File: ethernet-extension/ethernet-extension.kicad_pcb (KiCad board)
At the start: 2 copper layers, 56 x 30.4 mm, 43 parts, among them J1 Wuerth_7499010121A, J2 East, J3 West, U1 W5500, Y1 25MHz

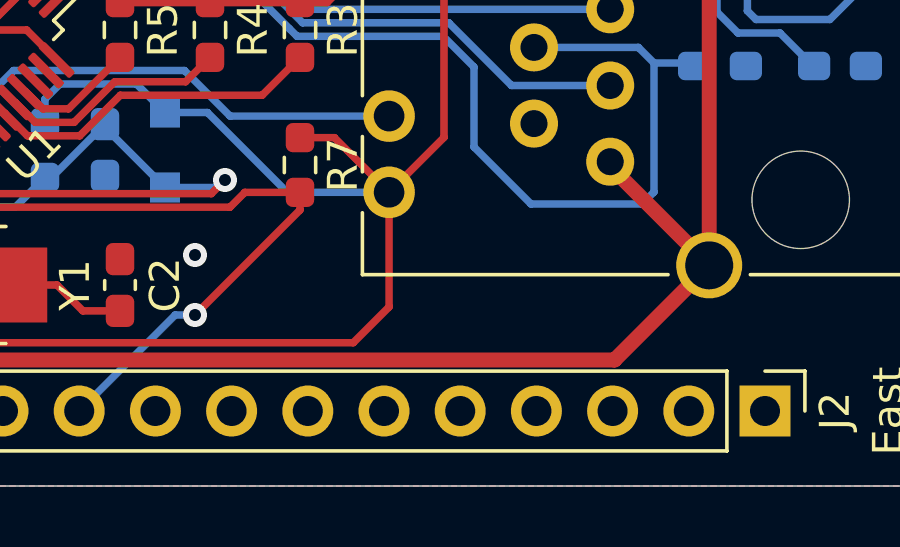
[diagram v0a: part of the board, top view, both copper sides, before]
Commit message: Added Panel Module to build
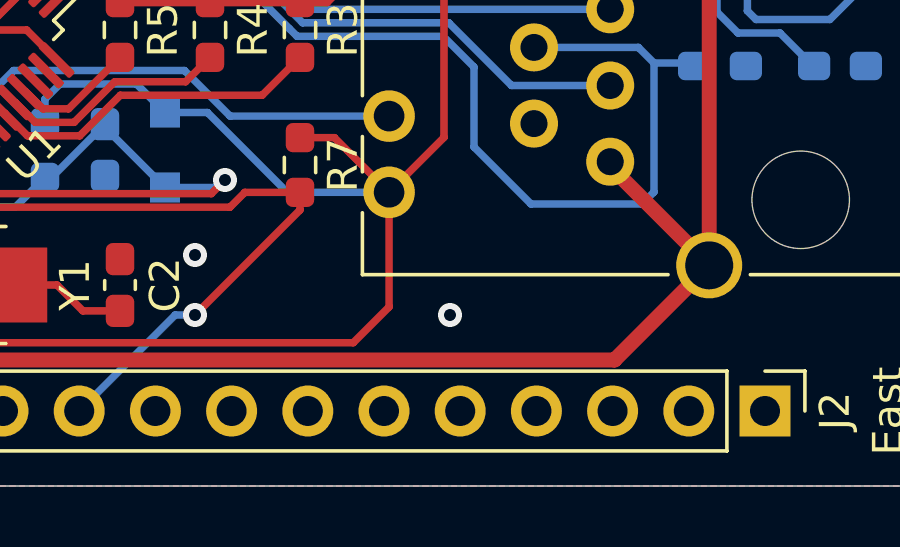
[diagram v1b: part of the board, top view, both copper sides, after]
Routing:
- net GND: vias 5 -> 6

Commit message: Added OpenHardware Logo to PCBs
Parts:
- added G2: Logo_Open_Hardware_Small, Symbol:OSHW-Logo2_7.3x6mm_SilkScreen, B.Cu at (152.5, 106.0)

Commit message: Migrate Ethernet, SoC, Metering Modules to KiCad6
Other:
- net class Default removed

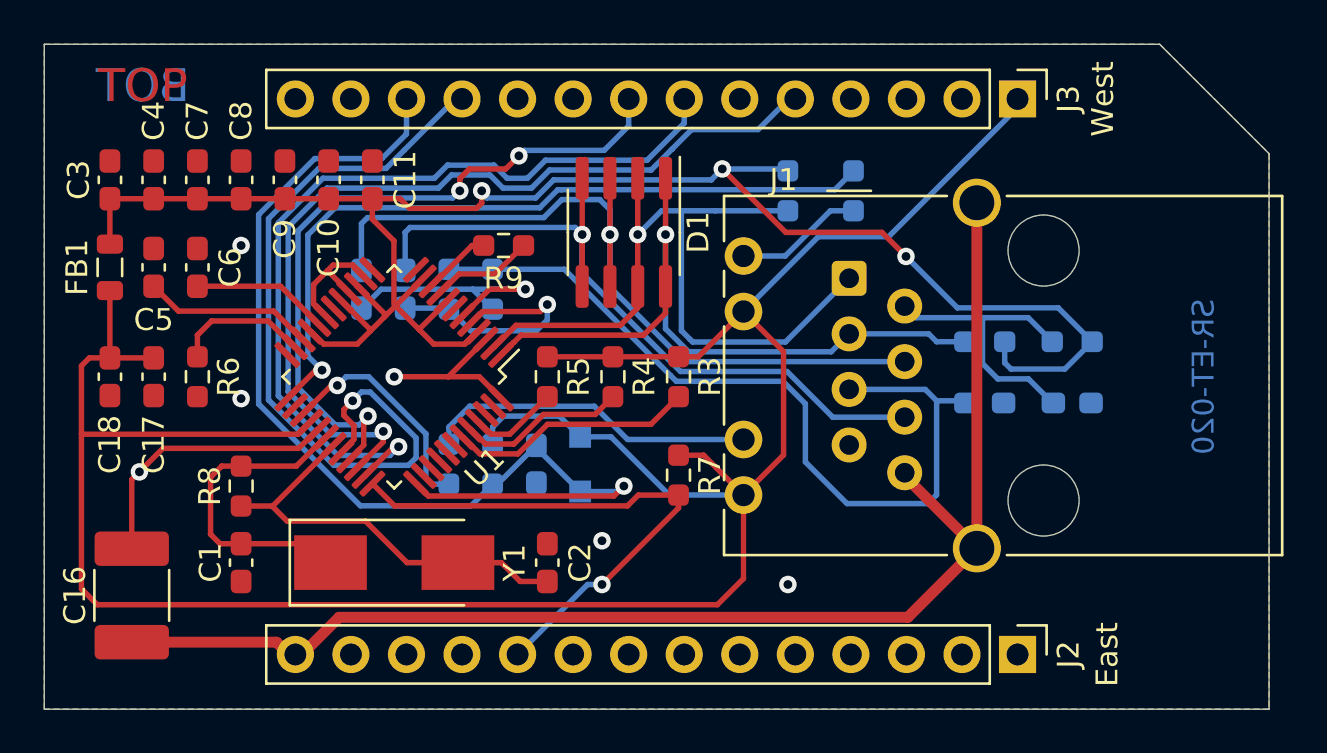
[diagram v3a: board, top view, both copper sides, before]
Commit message: Trim further warnings and errors
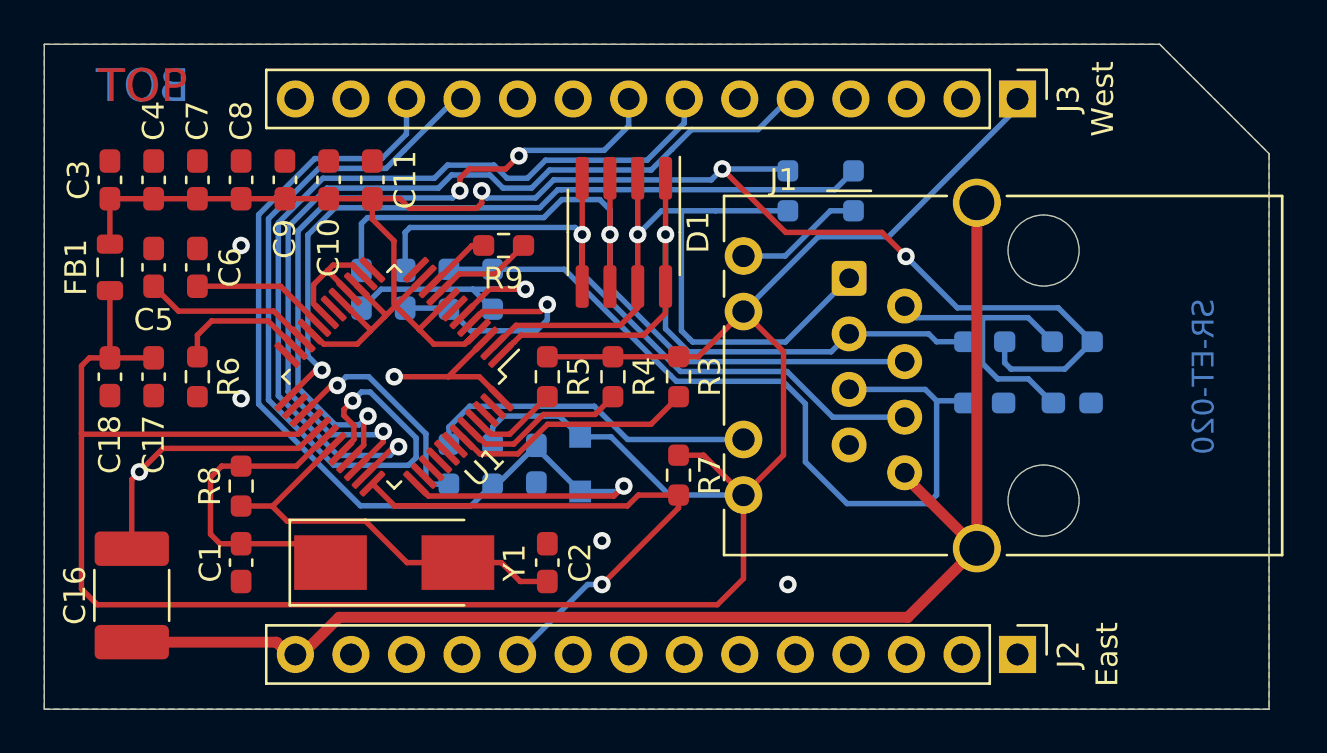
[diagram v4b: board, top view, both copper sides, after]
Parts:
- turned FB1 to 90 degrees
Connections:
- FB1 pad 1: +3.3VA -> +3V3
- FB1 pad 2: +3V3 -> +3.3VA
- J2 pad 11: Net-(J2-Pad11) -> unconnected-(J2-Pad11)
- J2 pad 12: Net-(J2-Pad12) -> unconnected-(J2-Pad12)
- J2 pad 13: Net-(J2-Pad13) -> unconnected-(J2-Pad13)
- J2 pad 2: Net-(J2-Pad2) -> unconnected-(J2-Pad2)
- J2 pad 3: Net-(J2-Pad3) -> unconnected-(J2-Pad3)
- J2 pad 4: Net-(J2-Pad4) -> unconnected-(J2-Pad4)
- J2 pad 5: Net-(J2-Pad5) -> unconnected-(J2-Pad5)
- J2 pad 6: Net-(J2-Pad6) -> unconnected-(J2-Pad6)
- J2 pad 7: Net-(J2-Pad7) -> unconnected-(J2-Pad7)
- J2 pad 8: Net-(J2-Pad8) -> unconnected-(J2-Pad8)
- J2 pad 9: Net-(J2-Pad9) -> unconnected-(J2-Pad9)
- J3 pad 10: Net-(J3-Pad10) -> unconnected-(J3-Pad10)
- J3 pad 13: Net-(J3-Pad13) -> unconnected-(J3-Pad13)
- J3 pad 14: Net-(J3-Pad14) -> unconnected-(J3-Pad14)
- J3 pad 2: Net-(J3-Pad2) -> unconnected-(J3-Pad2)
- J3 pad 3: Net-(J3-Pad3) -> unconnected-(J3-Pad3)
- J3 pad 4: Net-(J3-Pad4) -> unconnected-(J3-Pad4)
- J3 pad 6: Net-(J3-Pad6) -> unconnected-(J3-Pad6)
- J3 pad 9: Net-(J3-Pad9) -> unconnected-(J3-Pad9)
- U1 pad 12: Net-(U1-Pad12) -> unconnected-(U1-Pad12)
- U1 pad 13: Net-(U1-Pad13) -> unconnected-(U1-Pad13)
- U1 pad 18: Net-(U1-Pad18) -> unconnected-(U1-Pad18)
- U1 pad 24: Net-(U1-Pad24) -> unconnected-(U1-Pad24)
- U1 pad 26: Net-(U1-Pad26) -> unconnected-(U1-Pad26)
- U1 pad 38: Net-(U1-Pad38) -> unconnected-(U1-Pad38)
- U1 pad 39: Net-(U1-Pad39) -> unconnected-(U1-Pad39)
- U1 pad 40: Net-(U1-Pad40) -> unconnected-(U1-Pad40)
- U1 pad 41: Net-(U1-Pad41) -> unconnected-(U1-Pad41)
- U1 pad 42: Net-(U1-Pad42) -> unconnected-(U1-Pad42)
- U1 pad 46: Net-(U1-Pad46) -> unconnected-(U1-Pad46)
- U1 pad 47: Net-(U1-Pad47) -> unconnected-(U1-Pad47)
- U1 pad 7: Net-(U1-Pad7) -> unconnected-(U1-Pad7)
